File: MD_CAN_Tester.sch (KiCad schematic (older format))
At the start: 34 parts

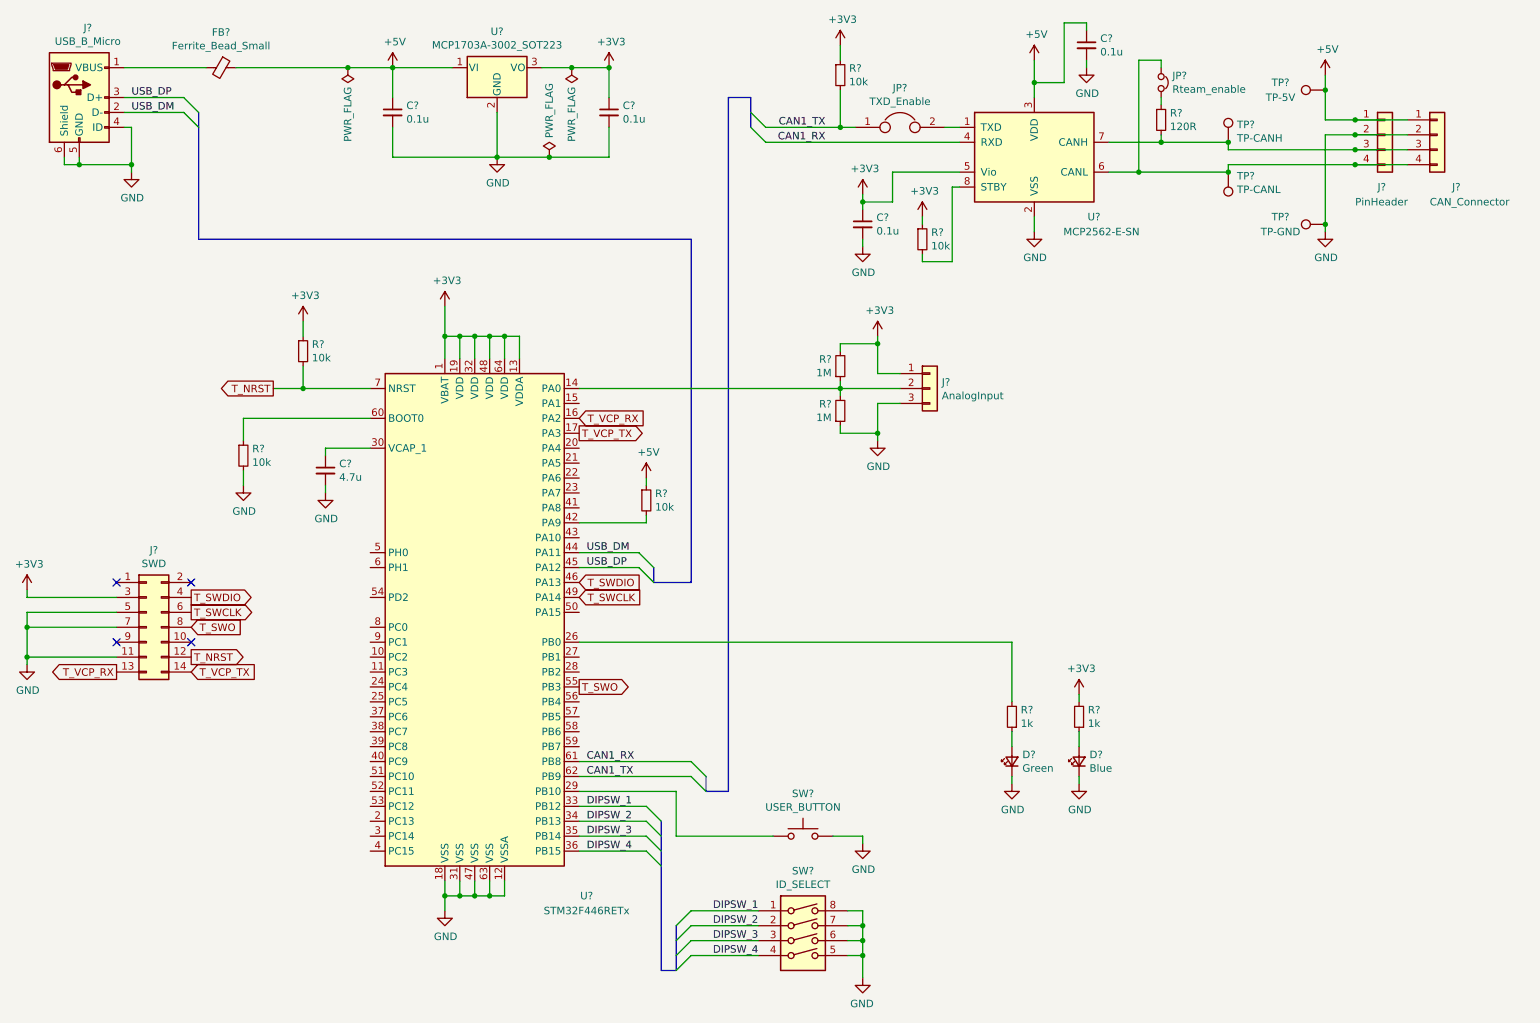
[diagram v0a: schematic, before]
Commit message: CAN5Vにジャンパ追加
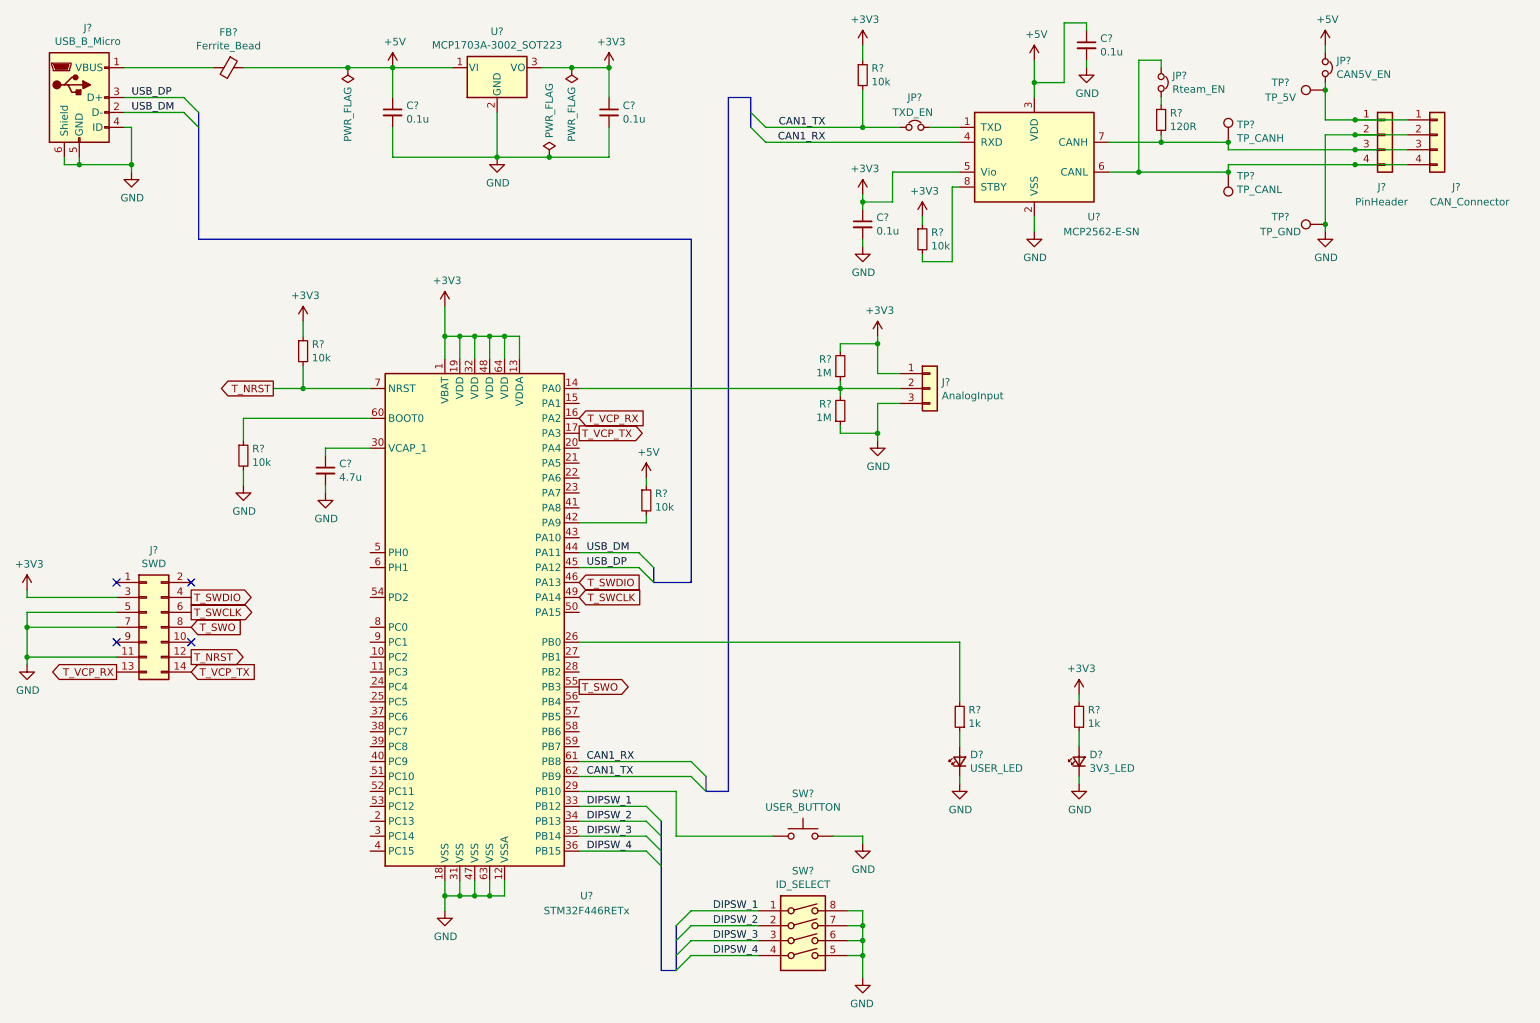
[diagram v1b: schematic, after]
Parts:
- removed JP?: TXD_Enable, symbol Device:Jumper
- added JP?: CAN5V_EN, symbol Device:Jumper_NC_Small
- added JP?: TXD_EN, symbol Device:Jumper_NC_Small
- D?: value Blue -> 3V3_LED
- D?: value Green -> USER_LED
- FB?: value Ferrite_Bead_Small -> Ferrite_Bead
- JP?: value Rteam_enable -> Rteam_EN
- TP?: value TP-CANH -> TP_CANH
- TP?: value TP-CANL -> TP_CANL
- TP?: value TP-GND -> TP_GND
- TP?: value TP-5V -> TP_5V
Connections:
- net +5V: now also JP?.1; no longer J?.1 (Pin_1), J?.1 (Pin_1), TP?.1
- net CAN1_TX: now also JP?.1
- net at U?.1 (TXD): now also JP?.2
- new net: J?.1 (Pin_1), J?.1 (Pin_1), JP?.2, TP?.1
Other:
- moved on the sheet: D?, FB?, R?
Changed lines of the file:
@@
-$EndComp
-$Comp
-L Device:Ferrite_Bead_Small FB?
-U 1 1 5F4D9268
-P 2300 1150
-F 0 "FB?" V 2063 1150 50  0000 C CNN
-F 1 "Ferrite_Bead_Small" V 2154 1150 50  0000 C CNN
-F 2 "" V 2230 1150 50  0001 C CNN
-F 3 "~" H 2300 1150 50  0001 C CNN
-	1    2300 1150
-	0    1    1    0
 $EndComp
 $Comp
@@
 $EndComp
 Wire Wire Line
-	2400 1150 3150 1150
+	2450 1150 3150 1150
 Wire Wire Line
 	3150 1150 3450 1150
@@
 Wire Wire Line
 	9700 1500 9900 1500
-Wire Wire Line
-	9700 1200 9700 1300
-$Comp
-L power:+5V #PWR?
-U 1 1 5F52B8C7
-P 9700 1200
-F 0 "#PWR?" H 9700 1050 50  0001 C CNN
-F 1 "+5V" H 9715 1373 50  0000 C CNN
-F 2 "" H 9700 1200 50  0001 C CNN
-F 3 "" H 9700 1200 50  0001 C CNN
-	1    9700 1200
-	1    0    0    -1
-$EndComp
 $Comp
 L Connector_Generic:Conn_01x04 J?
@@
 	6800 1850 7250 1850
 $Comp
-L Device:Jumper JP?
-U 1 1 5F55FA99
-P 6850 1550
-F 0 "JP?" H 6850 1814 50  0000 C CNN
-F 1 "TXD_Enable" H 6850 1723 50  0000 C CNN
-F 2 "" H 6850 1550 50  0001 C CNN
-F 3 "~" H 6850 1550 50  0001 C CNN
-	1    6850 1550
-	1    0    0    -1
-$EndComp
-$Comp
 L Device:R_Small R?
 U 1 1 5F5605D3
-P 6450 1200
-F 0 "R?" H 6509 1246 50  0000 L CNN
-F 1 "10k" H 6509 1155 50  0000 L CNN
-F 2 "" H 6450 1200 50  0001 C CNN
-F 3 "~" H 6450 1200 50  0001 C CNN
-	1    6450 1200
-	1    0    0    -1
-$EndComp
-Wire Wire Line
-	6450 1300 6450 1550
-Wire Wire Line
-	6550 1550 6450 1550
-Connection ~ 6450 1550
+P 6600 1200
+F 0 "R?" H 6659 1246 50  0000 L CNN
+F 1 "10k" H 6659 1155 50  0000 L CNN
+F 2 "" H 6600 1200 50  0001 C CNN
+F 3 "~" H 6600 1200 50  0001 C CNN
+	1    6600 1200
+	1    0    0    -1
+$EndComp
+Wire Wire Line
+	6600 1300 6600 1550
 $Comp
 L power:+3V3 #PWR?
 U 1 1 5F56909F
-P 6450 1000
-F 0 "#PWR?" H 6450 850 50  0001 C CNN
-F 1 "+3V3" H 6465 1173 50  0000 C CNN
-F 2 "" H 6450 1000 50  0001 C CNN
-F 3 "" H 6450 1000 50  0001 C CNN
-	1    6450 1000
-	1    0    0    -1
-$EndComp
-Wire Wire Line
-	6450 1000 6450 1100
-Wire Wire Line
-	7150 1550 7250 1550
+P 6600 1000
+F 0 "#PWR?" H 6600 850 50  0001 C CNN
+F 1 "+3V3" H 6615 1173 50  0000 C CNN
+F 2 "" H 6600 1000 50  0001 C CNN
+F 3 "" H 6600 1000 50  0001 C CNN
+	1    6600 1000
+	1    0    0    -1
+$EndComp
+Wire Wire Line
+	6600 1000 6600 1100
 $Comp
 L Connector:TestPoint TP?
@@
 P 9050 1650
 F 0 "TP?" H 9108 1768 50  0000 L CNN
-F 1 "TP-CANH" H 9108 1677 50  0000 L CNN
+F 1 "TP_CANH" H 9108 1677 50  0000 L CNN
 F 2 "" H 9250 1650 50  0001 C CNN
 F 3 "~" H 9250 1650 50  0001 C CNN
@@
 P 9050 1850
 F 0 "TP?" H 8992 1876 50  0000 R CNN
-F 1 "TP-CANL" H 8992 1967 50  0000 R CNN
+F 1 "TP_CANL" H 8992 1967 50  0000 R CNN
 F 2 "" H 9250 1850 50  0001 C CNN
 F 3 "~" H 9250 1850 50  0001 C CNN
@@
 P 9700 2200
 F 0 "TP?" V 9750 2500 50  0000 C CNN
-F 1 "TP-GND" V 9650 2500 50  0000 C CNN
+F 1 "TP_GND" V 9650 2500 50  0000 C CNN
 F 2 "" H 9900 2200 50  0001 C CNN
 F 3 "~" H 9900 2200 50  0001 C CNN
 	1    9700 2200
-	0    -1   -1   0
-$EndComp
-$Comp
-L Connector:TestPoint TP?
-U 1 1 5F599DE6
-P 9700 1300
-F 0 "TP?" V 9750 1600 50  0000 C CNN
-F 1 "TP-5V" V 9650 1600 50  0000 C CNN
-F 2 "" H 9900 1300 50  0001 C CNN
-F 3 "~" H 9900 1300 50  0001 C CNN
-	1    9700 1300
 	0    -1   -1   0
 $EndComp
@@
 	9050 1800 9900 1800
 Wire Wire Line
-	2200 1150 1650 1150
+	2250 1150 1650 1150
 $Comp
 L power:GND #PWR?
@@
 	5700 6000 5700 1350
 Wire Wire Line
-	5950 1550 6450 1550
-Wire Wire Line
 	5950 1650 7250 1650
 Entry Wire Line
@@
 P 8050 5800
 F 0 "D?" V 8096 5730 50  0000 R CNN
-F 1 "Blue" V 8005 5730 50  0000 R CNN
+F 1 "3V3_LED" V 8005 5730 50  0000 R CNN
 F 2 "" V 8050 5800 50  0001 C CNN
 F 3 "~" V 8050 5800 50  0001 C CNN
@@
 L Device:LED_Small D?
 U 1 1 5F86439A
-P 7600 5800
-F 0 "D?" V 7646 5730 50  0000 R CNN
-F 1 "Green" V 7555 5730 50  0000 R CNN
-F 2 "" V 7600 5800 50  0001 C CNN
-F 3 "~" V 7600 5800 50  0001 C CNN
-	1    7600 5800
+P 7250 5800
+F 0 "D?" V 7296 5730 50  0000 R CNN
+F 1 "USER_LED" V 7205 5730 50  0000 R CNN
+F 2 "" V 7250 5800 50  0001 C CNN
+F 3 "~" V 7250 5800 50  0001 C CNN
+	1    7250 5800
 	0    -1   -1   0
 $EndComp
@@
 L Device:R_Small R?
 U 1 1 5F8643A0
-P 7600 5500
-F 0 "R?" H 7541 5454 50  0000 R CNN
-F 1 "1k" H 7541 5545 50  0000 R CNN
-F 2 "" H 7600 5500 50  0001 C CNN
-F 3 "~" H 7600 5500 50  0001 C CNN
-	1    7600 5500
+P 7250 5500
+F 0 "R?" H 7191 5454 50  0000 R CNN
+F 1 "1k" H 7191 5545 50  0000 R CNN
+F 2 "" H 7250 5500 50  0001 C CNN
+F 3 "~" H 7250 5500 50  0001 C CNN
+	1    7250 5500
 	-1   0    0    1
 $EndComp
 Wire Wire Line
-	7600 5600 7600 5700
+	7250 5600 7250 5700
 $Comp
 L power:GND #PWR?
 U 1 1 5F87B57B
-P 7600 5950
-F 0 "#PWR?" H 7600 5700 50  0001 C CNN
-F 1 "GND" H 7605 5777 50  0000 C CNN
-F 2 "" H 7600 5950 50  0001 C CNN
-F 3 "" H 7600 5950 50  0001 C CNN
-	1    7600 5950
-	1    0    0    -1
-$EndComp
-Wire Wire Line
-	7600 5900 7600 5950
+P 7250 5950
+F 0 "#PWR?" H 7250 5700 50  0001 C CNN
+F 1 "GND" H 7255 5777 50  0000 C CNN
+F 2 "" H 7250 5950 50  0001 C CNN
+F 3 "" H 7250 5950 50  0001 C CNN
+	1    7250 5950
+	1    0    0    -1
+$EndComp
+Wire Wire Line
+	7250 5900 7250 5950
 $Comp
 L power:GND #PWR?
@@
 	5350 6000 5350 6300
 Wire Wire Line
-	7600 5000 7600 5400
-Wire Wire Line
-	4700 5000 7600 5000
+	7250 5000 7250 5400
+Wire Wire Line
+	4700 5000 7250 5000
 $Comp
 L power:GND #PWR?
@@
 P 8600 1250
 F 0 "JP?" V 8554 1325 50  0000 L CNN
-F 1 "Rteam_enable" V 8645 1325 50  0000 L CNN
+F 1 "Rteam_EN" V 8645 1325 50  0000 L CNN
 F 2 "" H 8600 1250 50  0001 C CNN
 F 3 "~" H 8600 1250 50  0001 C CNN
@@
 Wire Wire Line
 	9700 2200 9700 1600
-Connection ~ 9700 1300
-Wire Wire Line
-	9700 1300 9700 1500
 Wire Wire Line
 	8250 1650 8600 1650
@@
 Wire Wire Line
 	8450 1100 8450 1850
+Connection ~ 8450 1850
+Wire Wire Line
+	8450 1850 9050 1850
+$Comp
+L Device:Ferrite_Bead_Small FB?
+U 1 1 5F4D9268
+P 2350 1150
+F 0 "FB?" V 2113 1150 50  0000 C CNN
+F 1 "Ferrite_Bead" V 2204 1150 50  0000 C CNN
+F 2 "" V 2280 1150 50  0001 C CNN
+F 3 "~" H 2350 1150 50  0001 C CNN
+	1    2350 1150
+	0    1    1    0
+$EndComp
+$Comp
+L Device:Jumper_NC_Small JP?
+U 1 1 5F504CB1
+P 9700 1150
+F 0 "JP?" V 9654 1225 50  0000 L CNN
+F 1 "CAN5V_EN" V 9745 1225 50  0000 L CNN
+F 2 "" H 9700 1150 50  0001 C CNN
+F 3 "~" H 9700 1150 50  0001 C CNN
+	1    9700 1150
+	0    1    1    0
+$EndComp
+Wire Wire Line
+	9700 1250 9700 1300
+$Comp
+L power:+5V #PWR?
+U 1 1 5F52B8C7
+P 9700 1000
+F 0 "#PWR?" H 9700 850 50  0001 C CNN
+F 1 "+5V" H 9715 1173 50  0000 C CNN
+F 2 "" H 9700 1000 50  0001 C CNN
+F 3 "" H 9700 1000 50  0001 C CNN
+	1    9700 1000
+	1    0    0    -1
+$EndComp
+$Comp
+L Connector:TestPoint TP?
+U 1 1 5F599DE6
+P 9700 1300
+F 0 "TP?" V 9750 1600 50  0000 C CNN
+F 1 "TP_5V" V 9650 1600 50  0000 C CNN
+F 2 "" H 9900 1300 50  0001 C CNN
+F 3 "~" H 9900 1300 50  0001 C CNN
+	1    9700 1300
+	0    -1   -1   0
+$EndComp
+Connection ~ 9700 1300
+Wire Wire Line
+	9700 1300 9700 1500
+Wire Wire Line
+	9700 1000 9700 1050
+$Comp
+L Device:Jumper_NC_Small JP?
+U 1 1 5F548CF5
+P 6950 1550
+F 0 "JP?" H 6900 1750 50  0000 L CNN
+F 1 "TXD_EN" H 6800 1650 50  0000 L CNN
+F 2 "" H 6950 1550 50  0001 C CNN
+F 3 "~" H 6950 1550 50  0001 C CNN
+	1    6950 1550
+	1    0    0    -1
+$EndComp
+Wire Wire Line
+	7050 1550 7250 1550
+Connection ~ 6600 1550
+Wire Wire Line
+	6600 1550 6850 1550
+Wire Wire Line
+	5950 1550 6600 1550
 Wire Bus Line
 	5850 1350 5850 1550
@@
 Wire Bus Line
 	5250 6200 5250 7200
-Connection ~ 8450 1850
-Wire Wire Line
-	8450 1850 9050 1850
 $EndSCHEMATC

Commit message: Add: フットプリントの割り付け完了
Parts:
- C1, C2, C3, C4, C5: renamed from C?; footprint (none) -> Capacitor_SMD:C_0603_1608Metric
- D1, D2: renamed from D?; footprint (none) -> LED_SMD:LED_0603_1608Metric
- FB1: renamed from FB?; footprint (none) -> Inductor_SMD:L_0603_1608Metric
- J1: renamed from J?; footprint (none) -> LibLoader:ZX62R-B-5P
- J2: renamed from J?; footprint (none) -> LibLoader:FTSH-107-XX-YYY-DV-K-A-TR
- J3: renamed from J?; footprint (none) -> Connector_JST:JST_PH_B3B-PH-K_1x03_P2.00mm_Vertical
- J4: renamed from J?; footprint (none) -> Connector_PinHeader_2.54mm:PinHeader_1x04_P2.54mm_Vertical
- J5: renamed from J?; footprint (none) -> Connector_JST:JST_PH_B4B-PH-K_1x04_P2.00mm_Vertical
- JP1, JP2, JP3: renamed from JP?; footprint (none) -> Connector_PinHeader_2.54mm:PinHeader_1x02_P2.54mm_Vertical
- R1, R10, R2, R3, R4, R5, R6, R7, R8, R9: renamed from R?; footprint (none) -> Resistor_SMD:R_0603_1608Metric
- SW1: renamed from SW?; footprint (none) -> LibLoader:SKRPACE010
- SW2: renamed from SW?; footprint (none) -> LibLoader:SOIC127P812X230-8N
- TP1, TP2, TP3, TP4: renamed from TP?; footprint (none) -> TestPoint:TestPoint_Loop_D2.50mm_Drill1.0mm_LowProfile
- gave numbers to parts that had none: 3

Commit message: GND以外ほぼ配線済み
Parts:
- removed U2: MCP1703A-3002_SOT223, Package_TO_SOT_SMD:SOT-223-3_TabPin2, symbol Regulator_Linear:MCP1703A-3002_SOT223
- added C6, C7, C8, C9: 0.1u, Capacitor_SMD:C_0603_1608Metric, symbol Device:C_Small
- added R11, R12: 0R, Resistor_SMD:R_0603_1608Metric, symbol Device:R_Small
- added U2: MCP1703A-3302_SOT23, LibLoader:SOT95P255X145-3N, symbol Regulator_Linear:MCP1703A-3302_SOT23
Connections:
- net +3V3: now also C6.1, C7.1, C8.1, C9.1, U2.2 (VO)
- net +5V: now also U2.3 (VI)
- net GND: now also C6.2, C7.2, C8.2, C9.2, R11.2, R12.2, U2.1 (GND); no longer J1.4 (ID), J1.6 (Shield)
- new net: J1.4 (ID), R12.1
- new net: J1.6 (Shield), R11.1
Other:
- moved on the sheet: C2, C3
